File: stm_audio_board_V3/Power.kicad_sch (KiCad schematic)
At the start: 32 parts, among them U2 OP275, U3 MP-K7805-500R3, U4 OP275, U5 MIC2920A-3.3WS-TR, U6 L7809, U9 MIC2920A-3.3WS-TR

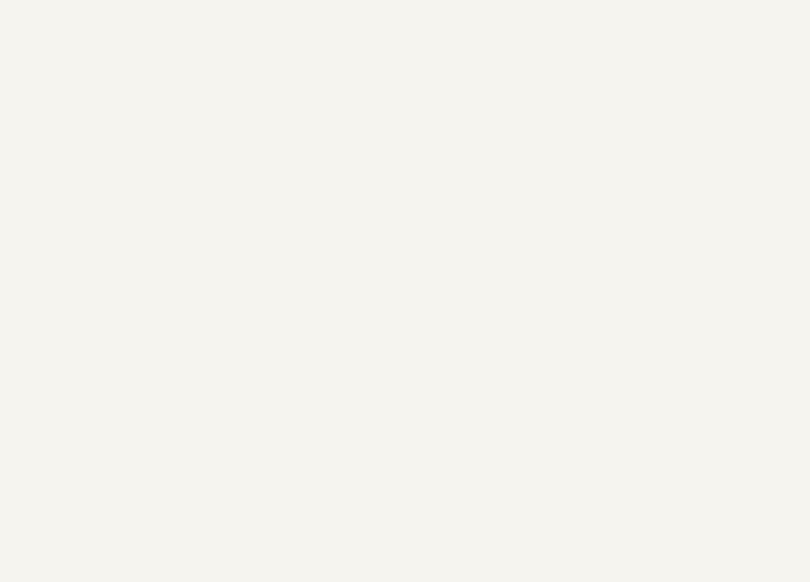
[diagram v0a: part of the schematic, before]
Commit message: SDRAM symbol added
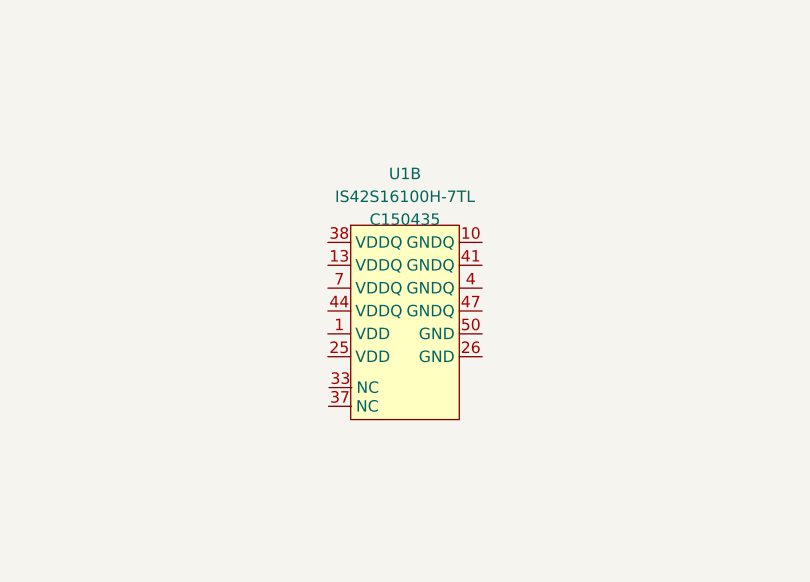
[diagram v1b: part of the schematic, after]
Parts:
- added U1: IS42S16100H-7TL, Package_SO:TSSOP-50_4.4x12.5mm_P0.5mm, symbol stm_audio:IS42S16100H-7TL
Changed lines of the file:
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@@
+    )
+  )
+  (symbol (lib_id "stm_audio:IS42S16100H-7TL") (at 66.04 158.75 0) (unit 2)
+    (in_bom yes) (on_board yes) (dnp no) (fields_autoplaced)
+    (property "Reference" "U1" (at 64.4525 148.59 0)
+      (effects (font (size 1.27 1.27)))
+    )
+    (property "Value" "IS42S16100H-7TL" (at 64.4525 151.13 0)
+      (effects (font (size 1.27 1.27)))
+    )
+    (property "Footprint" "Package_SO:TSSOP-50_4.4x12.5mm_P0.5mm" (at 53.975 154.94 0)
+      (effects (font (size 1.27 1.27)) hide)
+    )
+    (property "Datasheet" "https://jlcpcb.com/partdetail/161773-IS42S16100H7TL/C150435" (at 64.77 153.035 0)
+      (effects (font (size 1.27 1.27)) hide)
+    )
+    (property "JLCPCB" "C150435" (at 64.4525 153.67 0)
+      (effects (font (size 1.27 1.27)))
+    )
+    (pin "11")
+    (pin "12")
+    (pin "14")
+    (pin "15")
+    (pin "16")
+    (pin "17")
+    (pin "18")
+    (pin "19")
+    (pin "2")
+    (pin "20")
+    (pin "21")
+    (pin "22")
+    (pin "23")
+    (pin "24")
+    (pin "27")
+    (pin "28")
+    (pin "29")
+    (pin "3")
+    (pin "30")
+    (pin "31")
+    (pin "32")
+    (pin "34")
+    (pin "35")
+    (pin "36")
+    (pin "39")
+    (pin "40")
+    (pin "42")
+    (pin "43")
+    (pin "45")
+    (pin "46")
+    (pin "48")
+    (pin "49")
+    (pin "5")
+    (pin "6")
+    (pin "8")
+    (pin "9")
+    (pin "1")
+    (pin "10")
+    (pin "13")
+    (pin "25")
+    (pin "26")
+    (pin "33")
+    (pin "37")
+    (pin "38")
+    (pin "4")
+    (pin "41")
+    (pin "44")
+    (pin "47")
+    (pin "50")
+    (pin "7")
+    (instances
+      (project "stm_audio_board_V3"
+        (path "/6997cf63-2615-4e49-9471-e7da1b6bae71/51aec99e-3301-49b6-8e7f-31ba63a05d64"
+          (reference "U1") (unit 2)
+        )
+        (path "/6997cf63-2615-4e49-9471-e7da1b6bae71/2eb2ee8f-ab98-4666-97f0-bfacb073bc88"
+          (reference "U1") (unit 2)
+        )
+      )
     )
   )

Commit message: pcb redesign
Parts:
- U1: footprint Package_SO:TSSOP-50_4.4x12.5mm_P0.5mm -> Library:TSOP-2-50-new
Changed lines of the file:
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@@
       (effects (font (size 1.27 1.27)))
     )
-    (property "Footprint" "Package_SO:TSSOP-50_4.4x12.5mm_P0.5mm" (at 53.975 154.94 0)
-      (effects (font (size 1.27 1.27)) hide)
+    (property "Footprint" "Library:TSOP-2-50-new" (at 53.975 154.94 0)
+      (effects (font (size 1.27 1.27)))
     )
     (property "Datasheet" "https://jlcpcb.com/partdetail/161773-IS42S16100H7TL/C150435" (at 64.77 153.035 0)

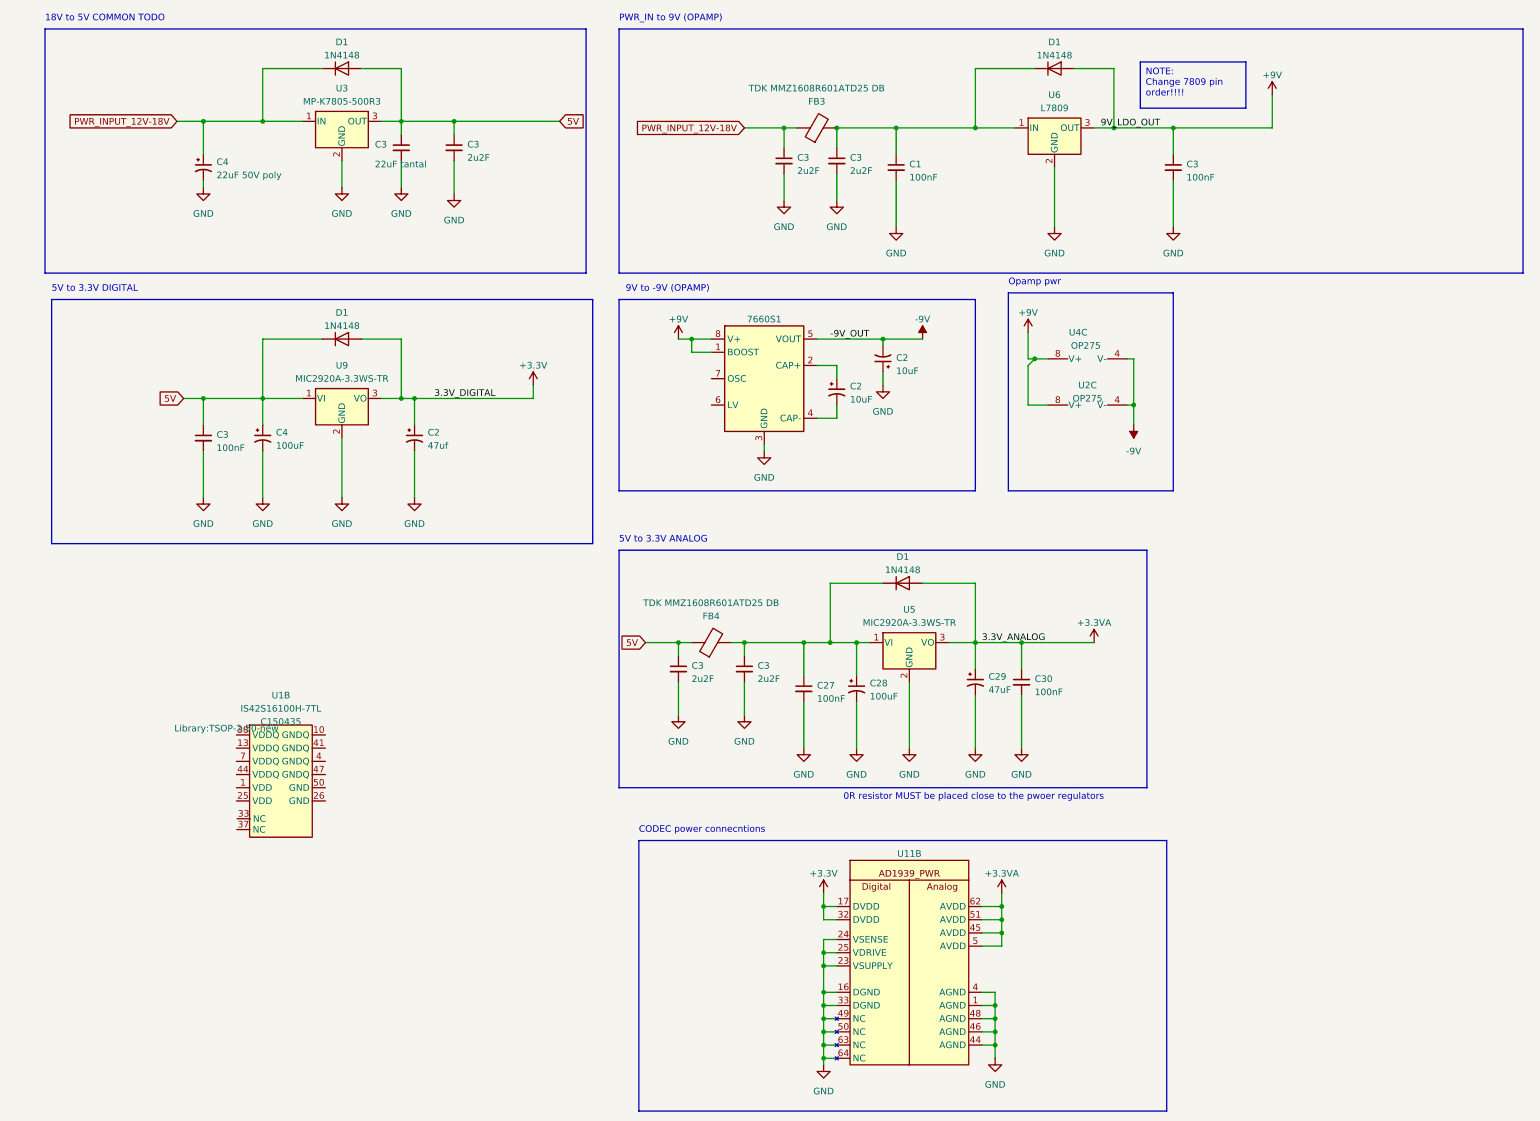
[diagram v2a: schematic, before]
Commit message: Input and output stages are made and assembly started on pcb view
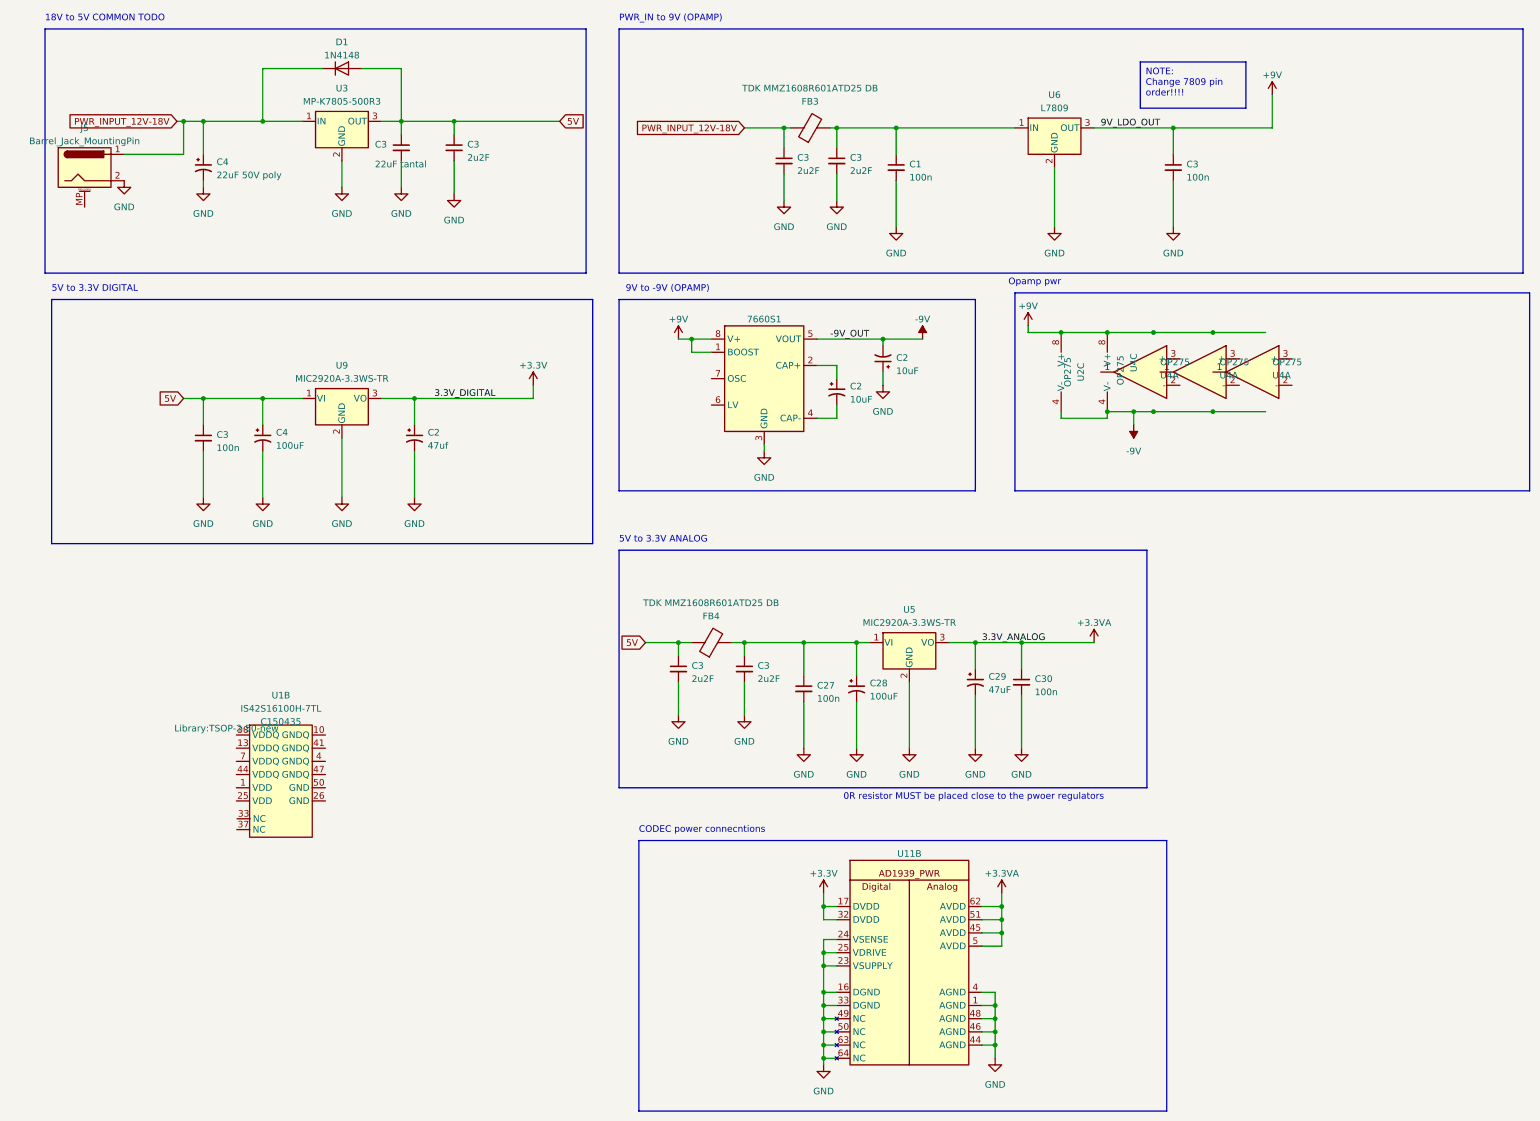
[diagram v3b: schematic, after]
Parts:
- removed D1 (x3): 1N4148, Diode_SMD:D_1206_3216Metric_Pad1.42x1.75mm_HandSolder, symbol Diode:1N4148
- added J5: Barrel_Jack_MountingPin, Connector_BarrelJack:BarrelJack_CUI_PJ-063AH_Horizontal, symbol Connector:Barrel_Jack_MountingPin
- added unit 1 of U4 (x3)
- C1, C27, C3, C30: value 100nF -> 100n; footprint Capacitor_SMD:C_0603_1608Metric_Pad1.08x0.95mm_HandSolder -> Capacitor_SMD:C_0603_1608Metric
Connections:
- net GND: now also J5.2
- net PWR_INPUT_12V-18V: now also J5.1
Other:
- moved on the sheet: FB3, U2C, U4C
